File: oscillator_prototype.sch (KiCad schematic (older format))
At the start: 94 parts, among them J1 shark fin, J10 Conn_01x06_Male, J11 Conn_01x06_Female, J12 Conn_01x06_Male, J13 Conn_01x06_Female, J14 Conn_01x06_Male, J3 1v/oct, J4 Triangle, J6 Sync, J7 Eurorack power, J8 Linear FM, J9 Conn_01x06_Female, Q1 MMBT3904, Q2 MMBT3906, Q3 BC857BS, Q4 MMBT3904, Q5 MMBT3904, SW1 Sync Mode, U1 LT1013-SOIC, U10 LM4040AIM3-5, U11 LM4040AIM3-5, U2 TL074, U3 LM13700, U4 LM311, U5 LM4040AIM3-2.5, U6 DG418, U7 LM311, U8 LM4040AIM3-2.5, U9 LM4040AIM3-2.5

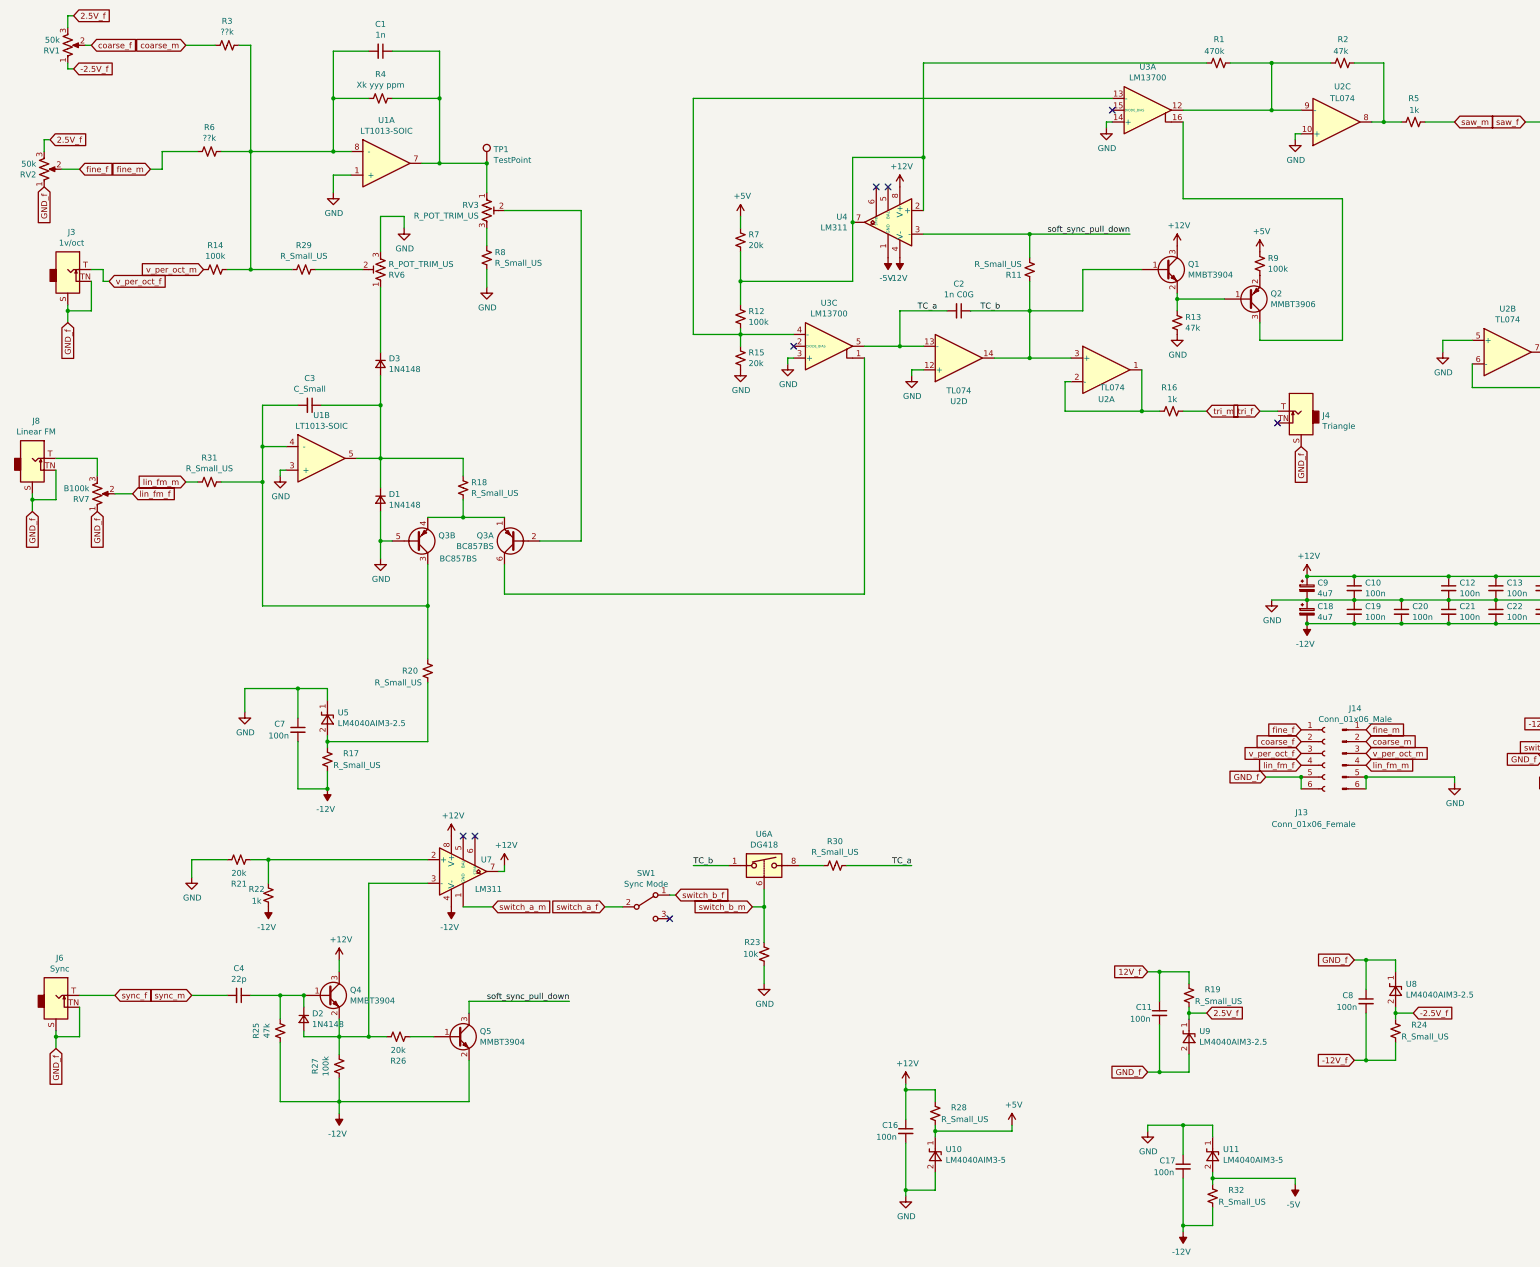
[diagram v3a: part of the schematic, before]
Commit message: Add all missing component values to schematic
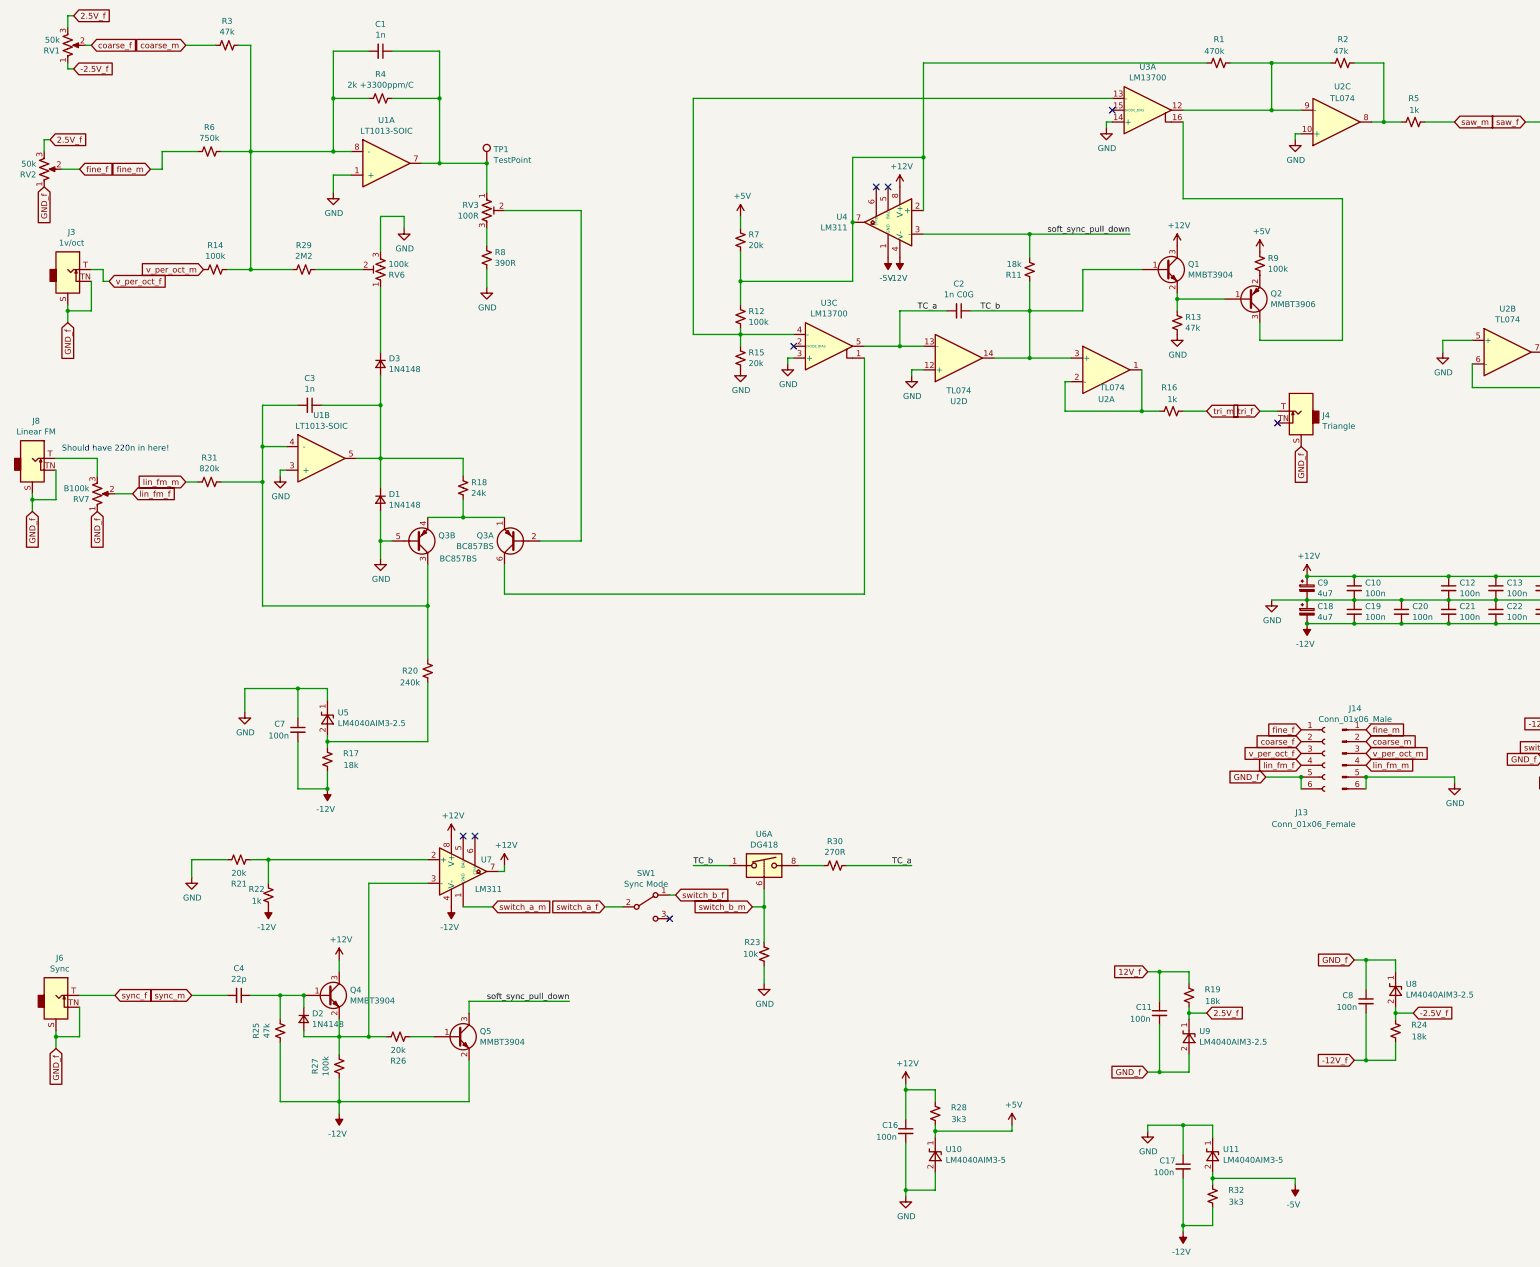
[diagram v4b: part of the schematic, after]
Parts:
- C3: value C_Small -> 1n
- R11, R17, R19, R24: value R_Small_US -> 18k
- R18: value R_Small_US -> 24k
- R20: value R_Small_US -> 240k
- R28, R32: value R_Small_US -> 3k3
- R29: value R_Small_US -> 2M2
- R3: value ??k -> 47k
- R30: value R_Small_US -> 270R
- R31: value R_Small_US -> 820k
- R4: value Xk yyy ppm -> 2k +3300ppm/C
- R6: value ??k -> 750k
- R8: value R_Small_US -> 390R
- RV3: value R_POT_TRIM_US -> 100R
- RV6: value R_POT_TRIM_US -> 100k
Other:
- note added: "Should have 220n in here!"
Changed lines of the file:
@@
 P 4350 4650
 F 0 "R18" H 4418 4696 50  0000 L CNN
-F 1 "R_Small_US" H 4418 4605 50  0000 L CNN
+F 1 "24k" H 4418 4605 50  0000 L CNN
 F 2 "Resistor_SMD:R_0805_2012Metric_Pad1.20x1.40mm_HandSolder" H 4350 4650 50  0001 C CNN
 F 3 "~" H 4350 4650 50  0001 C CNN
@@
 P 3050 3950
 F 0 "C3" V 2821 3950 50  0000 C CNN
-F 1 "C_Small" V 2912 3950 50  0000 C CNN
+F 1 "1n" V 2912 3950 50  0000 C CNN
 F 2 "Capacitor_SMD:C_0805_2012Metric_Pad1.18x1.45mm_HandSolder" H 3050 3950 50  0001 C CNN
 F 3 "~" H 3050 3950 50  0001 C CNN
@@
 P 4050 6200
 F 0 "R20" H 3900 6200 50  0000 C CNN
-F 1 "R_Small_US" H 3800 6100 50  0000 C CNN
+F 1 "240k" H 3900 6100 50  0000 C CNN
 F 2 "Resistor_SMD:R_0805_2012Metric_Pad1.20x1.40mm_HandSolder" H 4050 6200 50  0001 C CNN
 F 3 "~" H 4050 6200 50  0001 C CNN
@@
 P 4550 2300
 F 0 "RV3" H 4482 2346 50  0000 R CNN
-F 1 "R_POT_TRIM_US" H 4482 2255 50  0000 R CNN
+F 1 "100R" H 4482 2255 50  0000 R CNN
 F 2 "Potentiometer_THT:Potentiometer_Bourns_3266X_Horizontal" H 4550 2300 50  0001 C CNN
 F 3 "~" H 4550 2300 50  0001 C CNN
@@
 P 4550 2700
 F 0 "R8" H 4482 2654 50  0000 R CNN
-F 1 "R_Small_US" H 4482 2745 50  0000 R CNN
+F 1 "390R" H 4482 2745 50  0000 R CNN
 F 2 "Resistor_SMD:R_0805_2012Metric_Pad1.20x1.40mm_HandSolder" H 4550 2700 50  0001 C CNN
 F 3 "~" H 4550 2700 50  0001 C CNN
@@
 P 3650 1350
 F 0 "R4" V 3445 1350 50  0000 C CNN
-F 1 "Xk yyy ppm" V 3536 1350 50  0000 C CNN
+F 1 "2k +3300ppm/C" V 3536 1350 50  0000 C CNN
 F 2 "Resistor_THT:R_Axial_DIN0204_L3.6mm_D1.6mm_P5.08mm_Horizontal" H 3650 1350 50  0001 C CNN
 F 3 "~" H 3650 1350 50  0001 C CNN
@@
 Wire Wire Line
 	7750 5550 4700 5550
-$Comp
-L Device:R_Small_US R11
-U 1 1 5FBF69ED
-P 9150 2800
-F 0 "R11" H 9218 2846 50  0000 L CNN
-F 1 "R_Small_US" H 9218 2755 50  0000 L CNN
-F 2 "Resistor_SMD:R_0805_2012Metric_Pad1.20x1.40mm_HandSolder" H 9150 2800 50  0001 C CNN
-F 3 "~" H 9150 2800 50  0001 C CNN
-	1    9150 2800
-	-1   0    0    1
-$EndComp
 NoConn ~ 7850 2100
 NoConn ~ 7950 2100
@@
 P 2350 900
 F 0 "R3" V 2145 900 50  0000 C CNN
-F 1 "??k" V 2236 900 50  0000 C CNN
+F 1 "47k" V 2236 900 50  0000 C CNN
 F 2 "Resistor_SMD:R_0805_2012Metric_Pad1.20x1.40mm_HandSolder" H 2350 900 50  0001 C CNN
 F 3 "~" H 2350 900 50  0001 C CNN
@@
 P 2200 1800
 F 0 "R6" V 1995 1800 50  0000 C CNN
-F 1 "??k" V 2086 1800 50  0000 C CNN
+F 1 "750k" V 2086 1800 50  0000 C CNN
 F 2 "Resistor_SMD:R_0805_2012Metric_Pad1.20x1.40mm_HandSolder" H 2200 1800 50  0001 C CNN
 F 3 "~" H 2200 1800 50  0001 C CNN
@@
 P 3000 2800
 F 0 "R29" V 2795 2800 50  0000 C CNN
-F 1 "R_Small_US" V 2886 2800 50  0000 C CNN
+F 1 "2M2" V 2886 2800 50  0000 C CNN
 F 2 "Resistor_SMD:R_0805_2012Metric_Pad1.20x1.40mm_HandSolder" H 3000 2800 50  0001 C CNN
 F 3 "~" H 3000 2800 50  0001 C CNN
@@
 P 3650 2800
 F 0 "RV6" H 3582 2846 50  0000 R CNN
-F 1 "R_POT_TRIM_US" H 3582 2755 50  0000 R CNN
+F 1 "100k" H 3582 2755 50  0000 R CNN
 F 2 "Potentiometer_THT:Potentiometer_Bourns_3266X_Horizontal" H 3650 2800 50  0001 C CNN
 F 3 "~" H 3650 2800 50  0001 C CNN
@@
 P 2200 4600
 F 0 "R31" V 1995 4600 50  0000 C CNN
-F 1 "R_Small_US" V 2086 4600 50  0000 C CNN
+F 1 "820k" V 2086 4600 50  0000 C CNN
 F 2 "Resistor_SMD:R_0805_2012Metric_Pad1.20x1.40mm_HandSolder" H 2200 4600 50  0001 C CNN
 F 3 "~" H 2200 4600 50  0001 C CNN
@@
 P 10500 8950
 F 0 "R19" H 10700 9000 50  0000 C CNN
-F 1 "R_Small_US" H 10750 8900 50  0000 C CNN
+F 1 "18k" H 10700 8900 50  0000 C CNN
 F 2 "Resistor_SMD:R_0805_2012Metric_Pad1.20x1.40mm_HandSolder" H 10500 8950 50  0001 C CNN
 F 3 "~" H 10500 8950 50  0001 C CNN
@@
 P 7500 7850
 F 0 "R30" V 7295 7850 50  0000 C CNN
-F 1 "R_Small_US" V 7386 7850 50  0000 C CNN
+F 1 "270R" V 7386 7850 50  0000 C CNN
 F 2 "Resistor_SMD:R_0805_2012Metric_Pad1.20x1.40mm_HandSolder" H 7500 7850 50  0001 C CNN
 F 3 "~" H 7500 7850 50  0001 C CNN
@@
 P 12250 9250
 F 0 "R24" H 12450 9300 50  0000 C CNN
-F 1 "R_Small_US" H 12500 9200 50  0000 C CNN
+F 1 "18k" H 12450 9200 50  0000 C CNN
 F 2 "Resistor_SMD:R_0805_2012Metric_Pad1.20x1.40mm_HandSolder" H 12250 9250 50  0001 C CNN
 F 3 "~" H 12250 9250 50  0001 C CNN
@@
 P 3200 6950
 F 0 "R17" H 3400 7000 50  0000 C CNN
-F 1 "R_Small_US" H 3450 6900 50  0000 C CNN
+F 1 "18k" H 3400 6900 50  0000 C CNN
 F 2 "Resistor_SMD:R_0805_2012Metric_Pad1.20x1.40mm_HandSolder" H 3200 6950 50  0001 C CNN
 F 3 "~" H 3200 6950 50  0001 C CNN
@@
 P 8350 9950
 F 0 "R28" H 8550 10000 50  0000 C CNN
-F 1 "R_Small_US" H 8600 9900 50  0000 C CNN
+F 1 "3k3" H 8550 9900 50  0000 C CNN
 F 2 "Resistor_SMD:R_0805_2012Metric_Pad1.20x1.40mm_HandSolder" H 8350 9950 50  0001 C CNN
 F 3 "~" H 8350 9950 50  0001 C CNN
@@
 P 10700 10650
 F 0 "R32" H 10900 10700 50  0000 C CNN
-F 1 "R_Small_US" H 10950 10600 50  0000 C CNN
+F 1 "3k3" H 10900 10600 50  0000 C CNN
 F 2 "Resistor_SMD:R_0805_2012Metric_Pad1.20x1.40mm_HandSolder" H 10700 10650 50  0001 C CNN
 F 3 "~" H 10700 10650 50  0001 C CNN
@@
 $EndComp
 Connection ~ 4550 1900
+Text Notes 950  4350 0    50   ~ 0
+Should have 220n in here!
+$Comp
+L Device:R_Small_US R11
+U 1 1 5FBF69ED
+P 9150 2800
+F 0 "R11" H 9218 2846 50  0000 L CNN
+F 1 "18k" H 9218 2755 50  0000 L CNN
+F 2 "Resistor_SMD:R_0805_2012Metric_Pad1.20x1.40mm_HandSolder" H 9150 2800 50  0001 C CNN
+F 3 "~" H 9150 2800 50  0001 C CNN
+	1    9150 2800
+	-1   0    0    1
+$EndComp
 $EndSCHEMATC

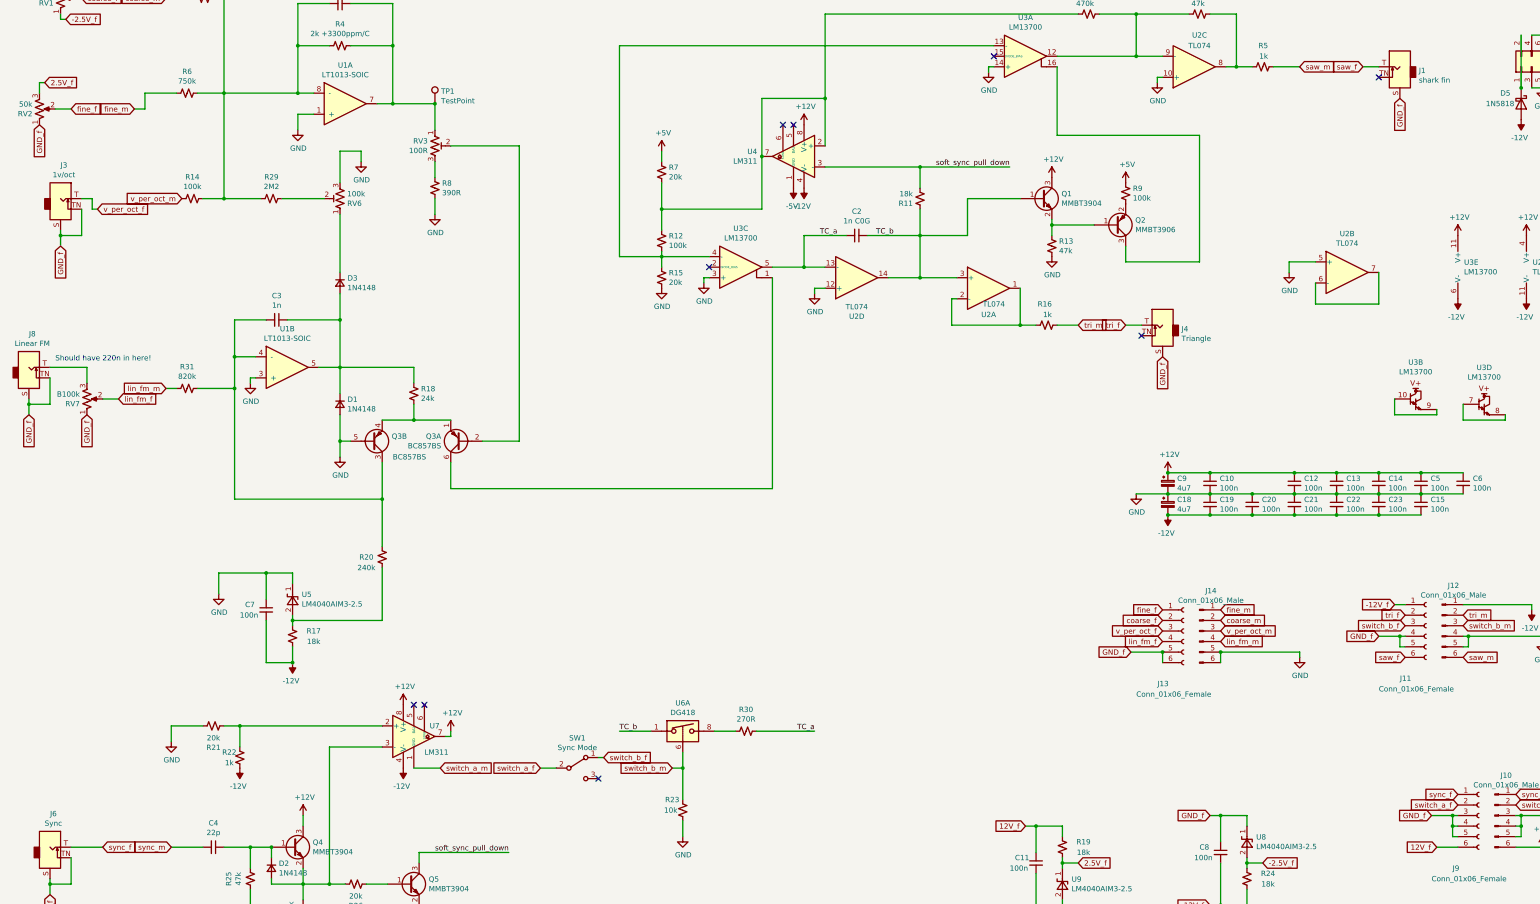
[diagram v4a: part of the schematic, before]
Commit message: Add BOM and panel
minor change to BOM to reduce part count
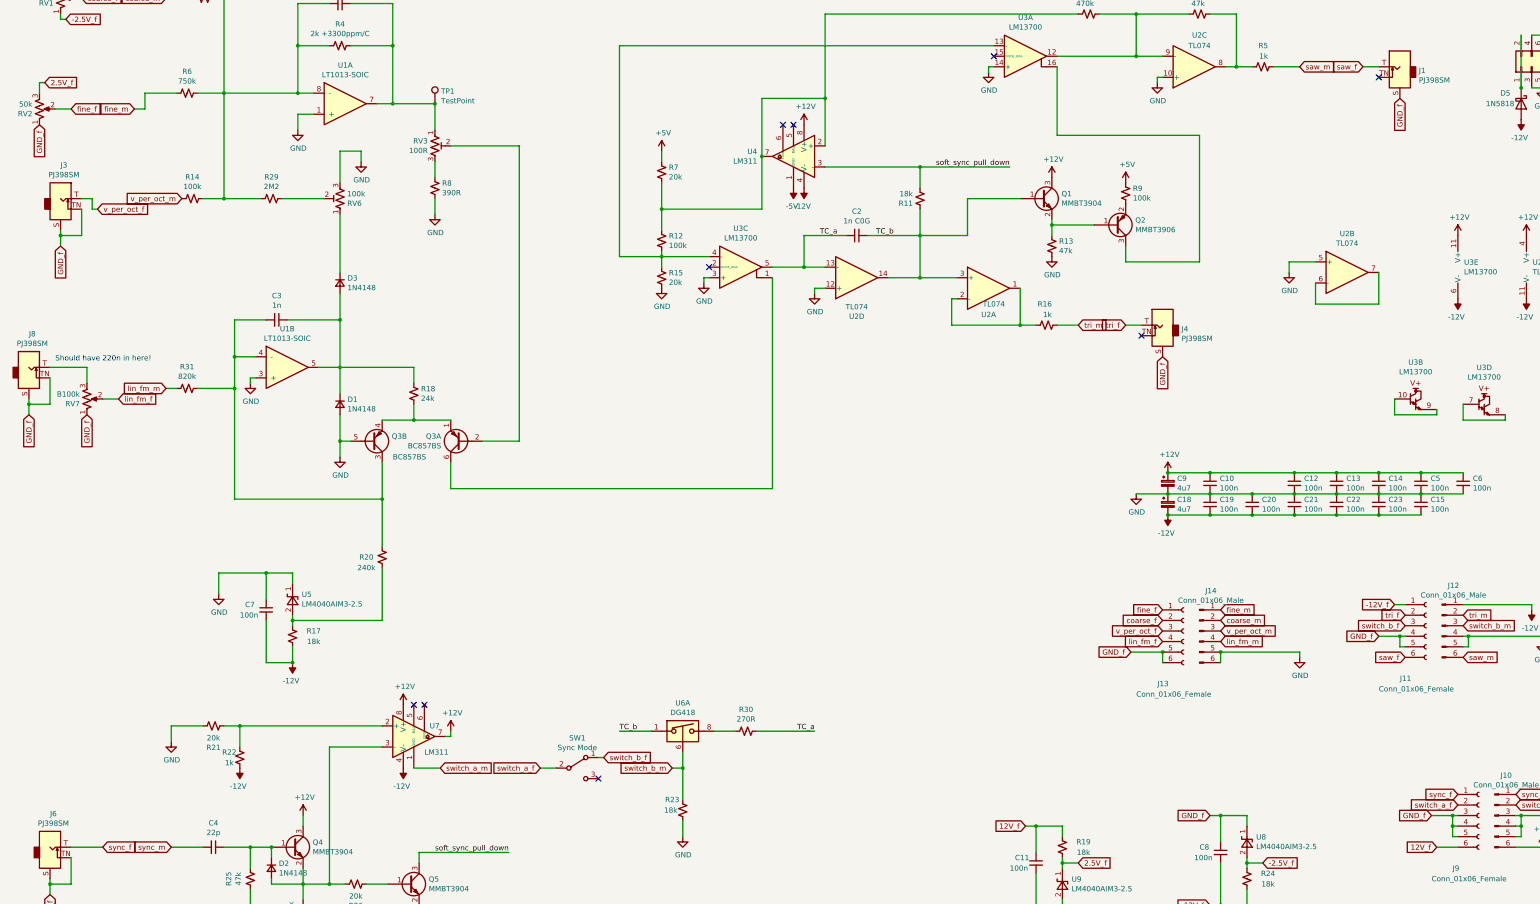
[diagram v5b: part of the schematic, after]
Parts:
- J1: value shark fin -> PJ398SM
- J3: value 1v/oct -> PJ398SM
- J4: value Triangle -> PJ398SM
- J6: value Sync -> PJ398SM
- J8: value Linear FM -> PJ398SM
- R23: value 10k -> 18k
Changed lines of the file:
@@
 P 900 8950
 F 0 "J6" H 932 9267 50  0000 C CNN
-F 1 "Sync" H 932 9176 50  0000 C CNN
+F 1 "PJ398SM" H 932 9176 50  0000 C CNN
 F 2 "kicad_libraries:Jack_3.5mm_QingPu_WQP-PJ398SM_Vertical_CircularHoles-translated" H 900 8950 50  0001 C CNN
 F 3 "" H 900 8950 50  0001 C CNN
@@
 P 13700 1550
 F 0 "J1" H 13520 1514 50  0000 R CNN
-F 1 "shark fin" H 13520 1423 50  0000 R CNN
+F 1 "PJ398SM" H 13520 1423 50  0000 R CNN
 F 2 "kicad_libraries:Jack_3.5mm_QingPu_WQP-PJ398SM_Vertical_CircularHoles-translated" H 13700 1550 50  0001 C CNN
 F 3 "" H 13700 1550 50  0001 C CNN
@@
 P 11450 4000
 F 0 "J4" H 11270 3964 50  0000 R CNN
-F 1 "Triangle" H 11270 3873 50  0000 R CNN
+F 1 "PJ398SM" H 11270 3873 50  0000 R CNN
 F 2 "kicad_libraries:Jack_3.5mm_QingPu_WQP-PJ398SM_Vertical_CircularHoles-translated" H 11450 4000 50  0001 C CNN
 F 3 "" H 11450 4000 50  0001 C CNN
@@
 P 1000 2800
 F 0 "J3" H 1032 3117 50  0000 C CNN
-F 1 "1v/oct" H 1032 3026 50  0000 C CNN
+F 1 "PJ398SM" H 1032 3026 50  0000 C CNN
 F 2 "kicad_libraries:Jack_3.5mm_QingPu_WQP-PJ398SM_Vertical_CircularHoles-translated" H 1000 2800 50  0001 C CNN
 F 3 "" H 1000 2800 50  0001 C CNN
@@
 P 700 4400
 F 0 "J8" H 732 4717 50  0000 C CNN
-F 1 "Linear FM" H 732 4626 50  0000 C CNN
+F 1 "PJ398SM" H 732 4626 50  0000 C CNN
 F 2 "kicad_libraries:Jack_3.5mm_QingPu_WQP-PJ398SM_Vertical_CircularHoles-translated" H 700 4400 50  0001 C CNN
 F 3 "" H 700 4400 50  0001 C CNN
@@
 P 6900 8600
 F 0 "R23" H 6800 8700 50  0000 C CNN
-F 1 "10k" H 6786 8600 50  0000 C CNN
+F 1 "18k" H 6786 8600 50  0000 C CNN
 F 2 "Resistor_SMD:R_0805_2012Metric_Pad1.20x1.40mm_HandSolder" H 6900 8600 50  0001 C CNN
 F 3 "~" H 6900 8600 50  0001 C CNN
